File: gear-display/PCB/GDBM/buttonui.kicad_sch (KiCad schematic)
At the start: 10 parts, among them M1 Knob_6mm_BL_RED_CLIFF_CL17084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, U5 Timer_Oscillator_TLC555CDG4

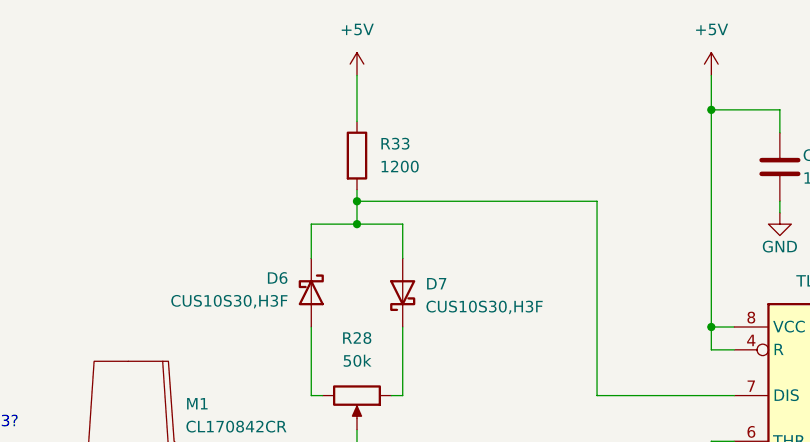
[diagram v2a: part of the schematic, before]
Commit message: R33 value change
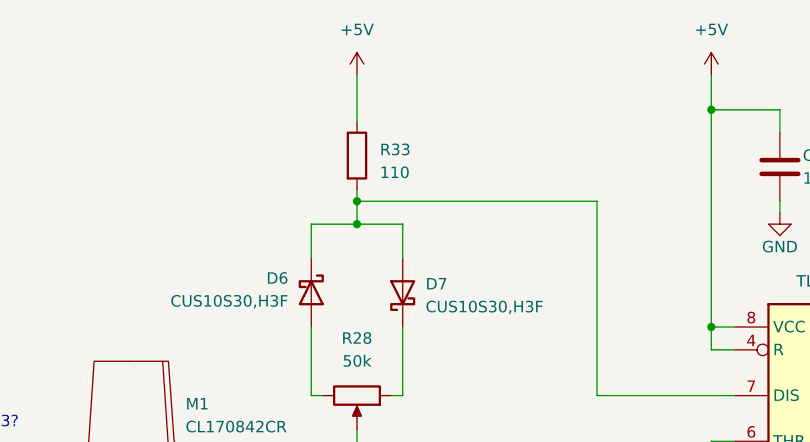
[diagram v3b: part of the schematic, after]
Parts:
- R33: value R_0805_1200_5% -> R_0805_110_5%; symbol KD_Resistor:R_0805_1200_5% -> KD_Resistor:R_0805_110_5%; Code 1200 -> 110; MFG_PartNo RMCF0805FT1K20 -> RMCF0805JT110R; Price 0.01 -> 0.005; Supplier_PartNo RMCF0805FT1K20CT-ND -> RMCF0805JT110RCT-ND
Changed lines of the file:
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@@
     )
   )
-  (symbol (lib_id "KD_Resistor:R_0805_1200_5%") (at 99.06 46.99 0) (unit 1)
+  (symbol (lib_id "KD_Resistor:R_0805_110_5%") (at 99.06 46.99 0) (unit 1)
     (in_bom yes) (on_board yes) (dnp no) (fields_autoplaced)
-    (property "Reference" "R33" (at 101.6 45.7199 0)
+    (property "Reference" "R33" (at 101.6 46.355 0)
       (effects (font (size 1.27 1.27)) (justify left))
     )
-    (property "Value" "R_0805_1200_5%" (at 86.36 15.24 0)
+    (property "Value" "R_0805_110_5%" (at 86.36 15.24 0)
       (effects (font (size 1.27 1.27)) (justify left) hide)
     )
@@
       (effects (font (size 1.27 1.27)) (justify left) hide)
     )
-    (property "Datasheet" "https://www.seielect.com/catalog/sei-rmcf_rmcp.pdf" (at 86.36 35.56 0)
+    (property "Datasheet" "https://www.seielect.com/Catalog/SEI-RMCF_RMCP.pdf" (at 86.36 35.56 0)
       (effects (font (size 1.27 1.27)) (justify left) hide)
     )
-    (property "Code" "1200" (at 101.6 48.2599 0)
+    (property "Code" "110" (at 101.6 48.895 0)
       (effects (font (size 1.27 1.27)) (justify left))
     )
@@
       (effects (font (size 1.27 1.27)) (justify left) hide)
     )
-    (property "MFG_PartNo" "RMCF0805FT1K20" (at 86.36 20.32 0)
+    (property "MFG_PartNo" "RMCF0805JT110R" (at 86.36 20.32 0)
       (effects (font (size 1.27 1.27)) (justify left) hide)
     )
@@
       (effects (font (size 1.27 1.27)) (justify left) hide)
     )
-    (property "Supplier_PartNo" "RMCF0805FT1K20CT-ND" (at 86.36 25.4 0)
+    (property "Supplier_PartNo" "RMCF0805JT110RCT-ND" (at 86.36 25.4 0)
       (effects (font (size 1.27 1.27)) (justify left) hide)
     )
@@
       (effects (font (size 1.27 1.27)) (justify left) hide)
     )
-    (property "Price" "0.01" (at 86.36 30.48 0)
+    (property "Price" "0.005" (at 86.36 30.48 0)
       (effects (font (size 1.27 1.27)) (justify left) hide)
     )

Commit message: updates
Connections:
- net at R33.2, U5.7 (DIS): now also D6.2 (A), D7.1 (K); no longer D6.1 (K), D7.2 (A)
- net at R28.1: now also D7.2 (A); no longer D7.1 (K)
- net at R28.3: now also D6.1 (K); no longer D6.2 (A)
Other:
- moved on the sheet: C21, C23, C24, M1, R28, R29, R33, U5

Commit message: Layout
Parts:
- C21: value C_0805_1u_X7R_25V -> 1u; Manufacturer Kemet -> Samsung Electro-Mechanics
- C23, C24: value C_0603_10n_X7R_100V -> 10n
- R28: value Pot_V_10k_CUI_PT01-D120K2-B103 -> PT01-D225D-A503
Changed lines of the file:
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@@
       (effects (font (size 1.27 1.27)) (justify right))
     )
-    (property "Value" "C_0603_10n_X7R_100V" (at 133.35 138.43 0)
+    (property "Value" "10n" (at 133.35 138.43 0)
       (effects (font (size 1.27 1.27)) (justify left) hide)
     )
@@
       (effects (font (size 1.27 1.27)) (justify left) hide)
     )
-    (property "Datasheet" "" (at 133.35 118.11 0)
+    (property "Datasheet" "datasheet" (at 133.35 118.11 0)
       (effects (font (size 1.27 1.27)) (justify left) hide)
     )
@@
       (effects (font (size 1.27 1.27)))
     )
-    (property "Value" "Pot_V_10k_CUI_PT01-D120K2-B103" (at 152.4 81.28 0)
+    (property "Value" "PT01-D225D-A503" (at 152.4 81.28 0)
       (effects (font (size 1.27 1.27)) (justify left) hide)
     )
@@
       (effects (font (size 1.27 1.27)))
     )
-    (property "Value" "C_0603_10n_X7R_100V" (at 163.83 111.76 0)
+    (property "Value" "10n" (at 163.83 111.76 0)
       (effects (font (size 1.27 1.27)) (justify left) hide)
     )
@@
       (effects (font (size 1.27 1.27)) (justify left) hide)
     )
-    (property "Datasheet" "" (at 184.15 111.76 0)
+    (property "Datasheet" "datasheet" (at 184.15 111.76 0)
       (effects (font (size 1.27 1.27)) (justify left) hide)
     )
@@
       (effects (font (size 1.27 1.27)) (justify left))
     )
-    (property "Value" "C_0805_1u_X7R_25V" (at 154.94 36.83 0)
+    (property "Value" "1u" (at 154.94 36.83 0)
       (effects (font (size 1.27 1.27)) (justify left) hide)
     )
@@
       (effects (font (size 1.27 1.27)) (justify left) hide)
     )
-    (property "Datasheet" "https://api.kemet.com/component-edge/download/datasheet/CBR08C279B5GAC.pdf" (at 154.94 57.15 0)
+    (property "Datasheet" "https://mm.digikey.com/Volume0/opasdata/d220001/medias/docus/1105/CL21B105KAFNNNE_Spec.pdf" (at 154.94 57.15 0)
       (effects (font (size 1.27 1.27)) (justify left) hide)
     )
@@
       (effects (font (size 1.27 1.27)) (justify left))
     )
-    (property "Manufacturer" "Kemet" (at 154.94 39.37 0)
-      (effects (font (size 1.27 1.27)) (justify left) hide)
-    )
+    (property "Manufacturer" "Samsung Electro-Mechanics" (at 154.94 39.37 0)
+      (effects (font (size 1.27 1.27)) (justify left) hide)
+    )
